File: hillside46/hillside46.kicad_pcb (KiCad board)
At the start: 2 copper layers, 142.5 x 99.9 mm, 86 parts, among them J1 Haptic, J2 TRRS, J3 Bat_Pos, J4 Bat_Neg, J5 Bat_Pos, J6 Bat_Neg, K1 SW_Key, K10 SW_Key, K11 SW_Key, K12 SW_Key, K13 SW_Key, K14 SW_Key, K15 SW_Key, K16 SW_Key, K17 SW_Key, K18 SW_Key, K19 SW_Rotary, K2 SW_Key, K20 SW_Rotary, K21 SW_Key, K22 SW_Key, K23 SW_Key, K3 SW_Key, K4 SW_Key, K5 SW_Key, K6 SW_Key, K7 SW_Key, K8 SW_Key, K9 SW_Key, SW1 SKQGAFE010, SW2 SW_Power, U1 ProMicro_r, U2 SRV05-4

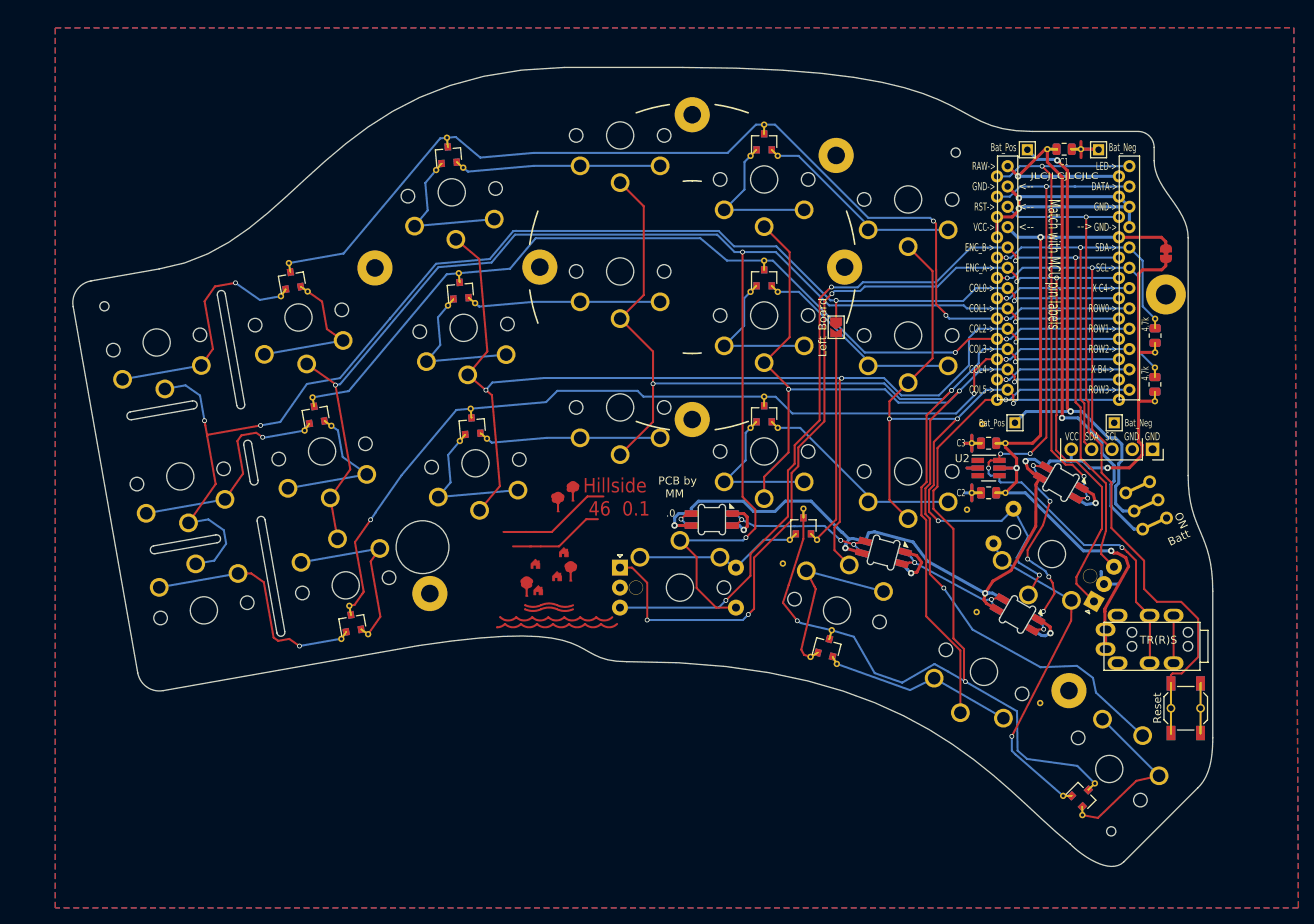
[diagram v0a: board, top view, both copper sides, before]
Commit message: 46 PCB: Ground plane and trace cleanups
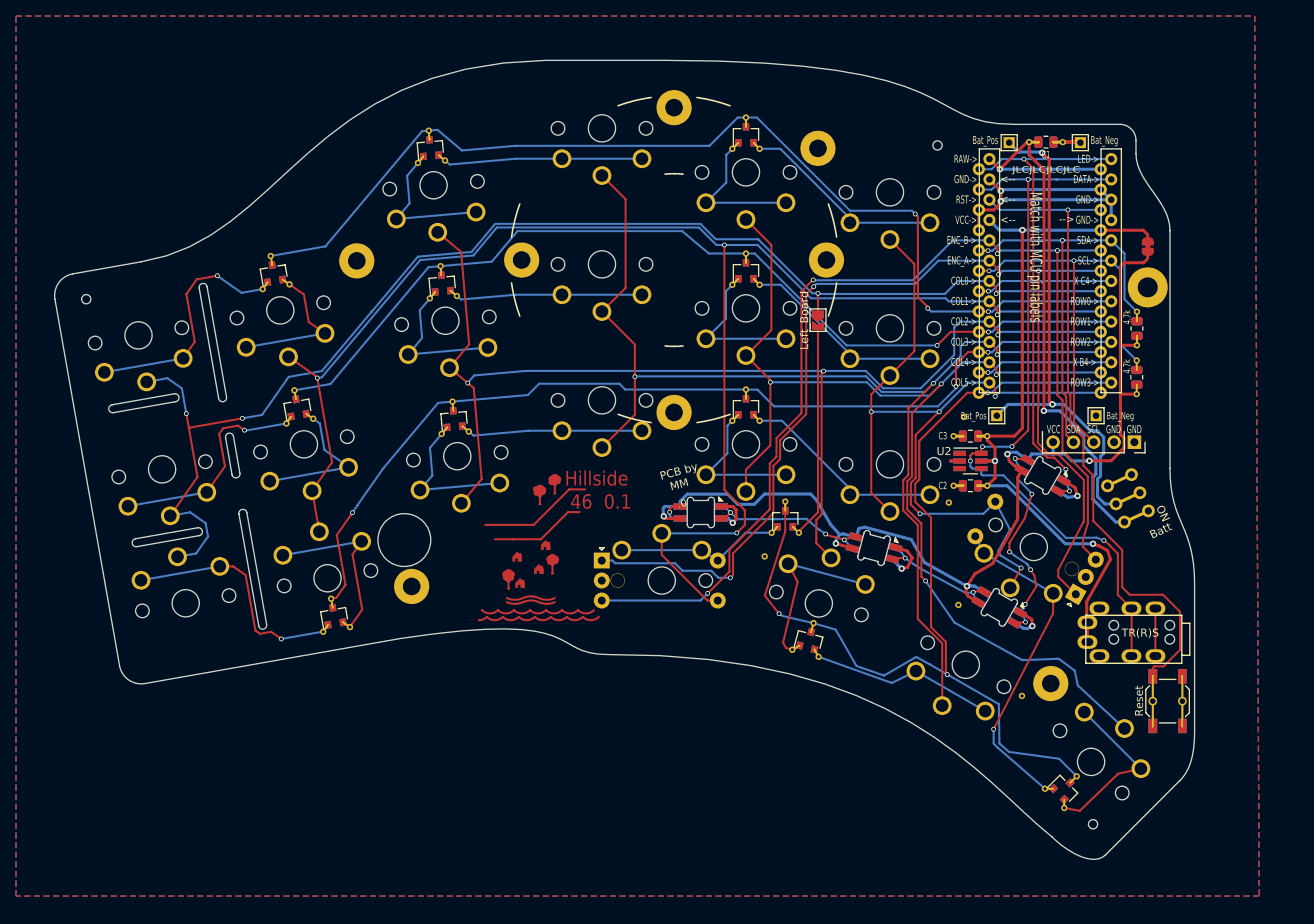
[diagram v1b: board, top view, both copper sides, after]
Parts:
- moved H15 2.93 mm to (93.2, 76.7)
- moved H19 2.73 mm to (194.9, 134.2)
- moved H16 2.65 mm to (203.1, 142.6)
- moved H14 2.61 mm to (132.8, 54.6)
- moved H12 2.57 mm to (88.1, 122.0)
- moved H10 2.48 mm to (80.5, 79.1)
- moved D7 2.44 mm to (101.8, 75.4)
- moved JP1 2.44 mm to (211.1, 72.1)
- moved K19 2.44 mm to (199.1, 105.7)
- moved K21 2.44 mm to (170.0, 116.7)
- moved K22 2.44 mm to (188.4, 124.3)
- moved V5 2.44 mm to (163.2, 110.8)
- moved K5 2.44 mm to (160.9, 62.8)
- moved D13 2.44 mm to (109.4, 118.2)
- moved K3 2.44 mm to (121.8, 64.4)
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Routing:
- net GND: track 85.9 -> 71.6 mm
- net enc_a: track 149.9 -> 141.4 mm, vias 5 -> 4
- net VCC: track 93.2 -> 92.0 mm
- net Net-(D2-Pad2): track 17.3 -> 16.2 mm
- net col1: track 194.3 -> 195.3 mm
- net reset: track 82.4 -> 83.1 mm

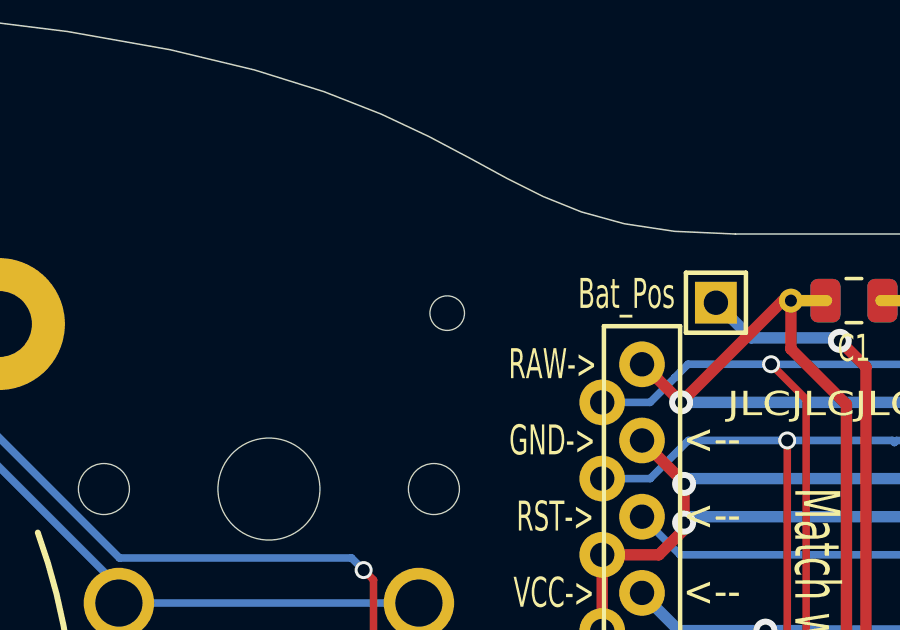
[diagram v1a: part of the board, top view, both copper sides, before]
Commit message: 46 PCB: trace cleanups
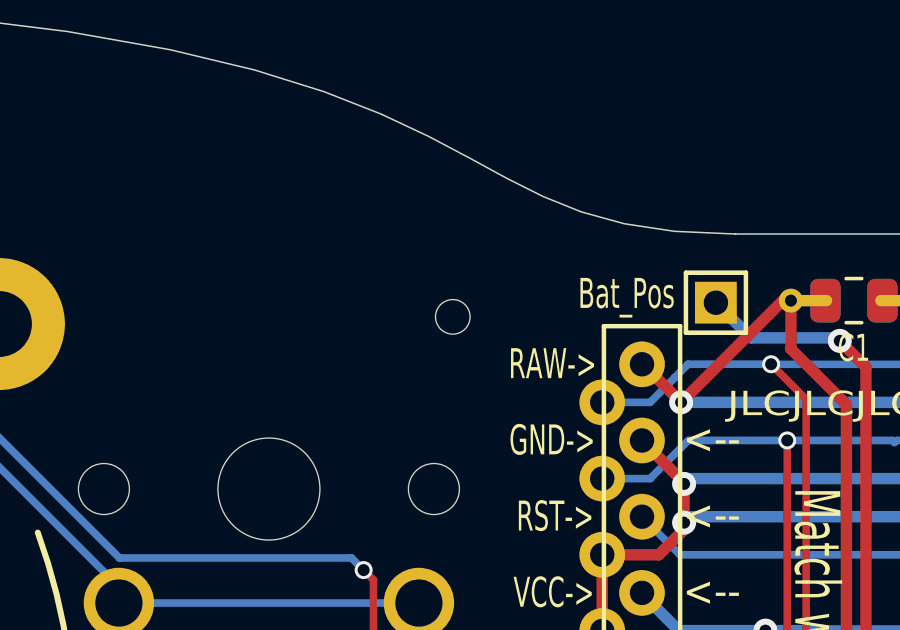
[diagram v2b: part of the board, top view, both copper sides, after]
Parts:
- moved H23 0.22 mm to (185.0, 59.6)
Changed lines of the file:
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@@
   )
   (footprint "hillside_basic:ToolingHole_1.152mm" (layer "F.Cu")
-    (at 184.818727 59.429153)
+    (at 185.004829 59.553153)
     (descr "Mounting Hole 2.1mm, no annular")
     (tags "mounting hole 2.1mm no annular")

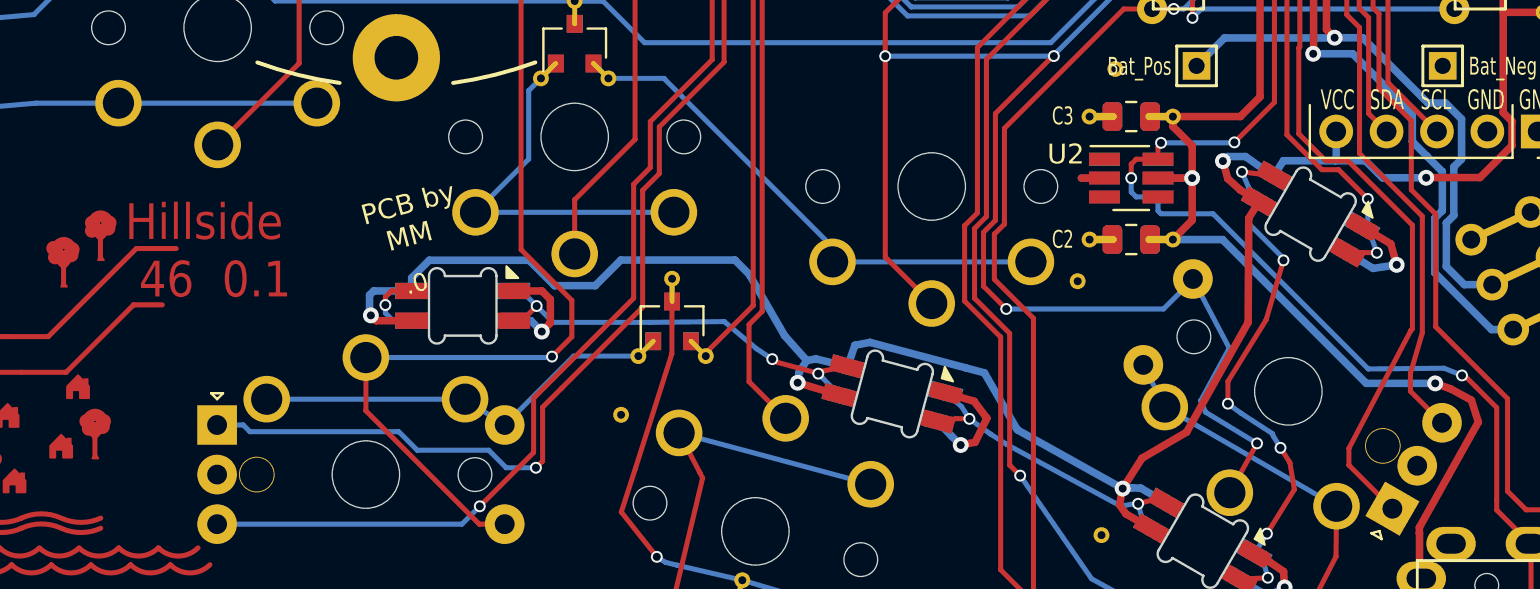
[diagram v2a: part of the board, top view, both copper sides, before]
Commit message: 46: PCB connect ground on encoder. Silk tweaks
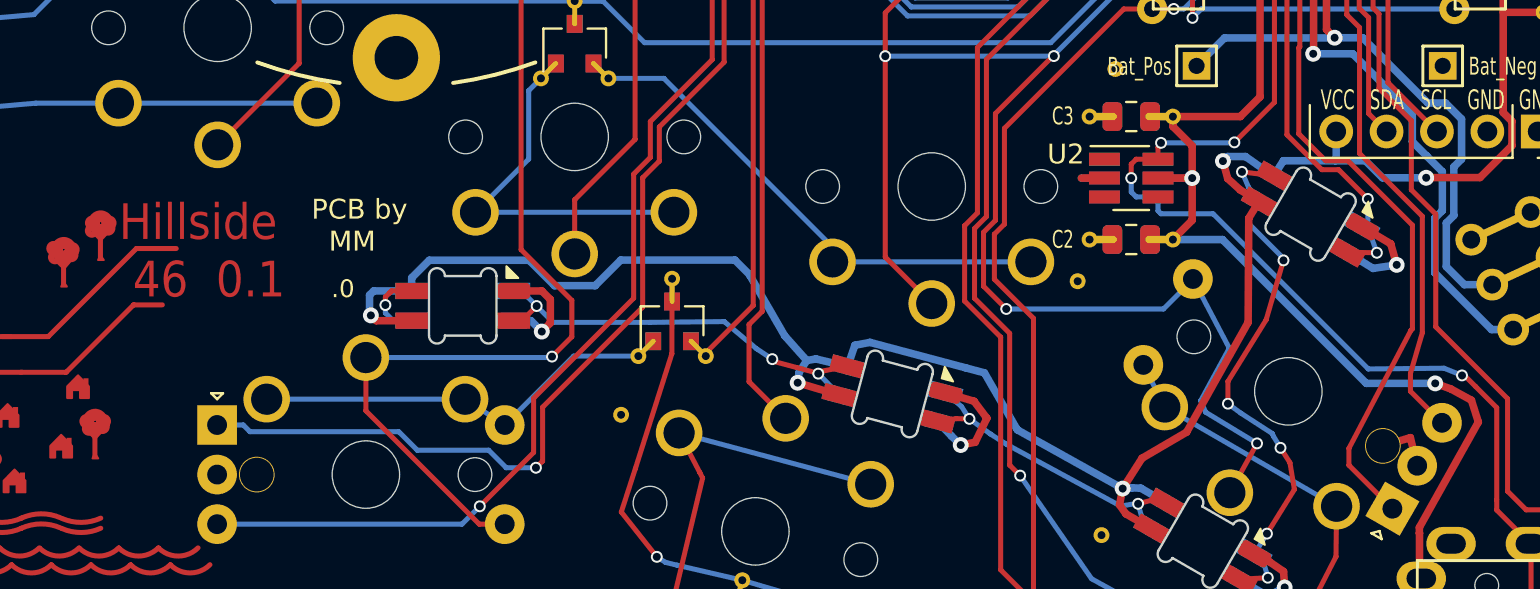
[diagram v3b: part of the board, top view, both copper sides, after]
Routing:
- net GND: track 71.6 -> 74.5 mm
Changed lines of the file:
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@@
   (gr_curve (pts (xy 205.821011 148.110245) (xy 204.095766 149.772261) (xy 200.565772 147.312259) (xy 199.140774 145.87226)) (layer "Edge.Cuts") (width 0.05))
   (gr_arc (start 74.498279 78.666546) (mid 74.953852 76.611692) (end 76.728967 75.480796) (layer "Edge.Cuts") (width 0.05))
-  (gr_text "Hillside \n 46  0.1" (at 138.204829 102.553153) (layer "F.Cu")
+  (gr_text "Hillside \n 46  0.1" (at 137.904829 102.553153) (layer "F.Cu")
     (effects (font (size 1.8 1.6) (thickness 0.24)) (justify left))
   )
-  (gr_text ".0" (at 152.336649 104.340041 15) (layer "F.SilkS")
+  (gr_text ".0" (at 148.604829 104.453153) (layer "F.SilkS")
     (effects (font (size 0.9 0.9) (thickness 0.153)) (justify left))
   )
-  (gr_text "PCB by\n  MM" (at 150.345613 101.562762 15) (layer "F.SilkS")
+  (gr_text "PCB by\n  MM" (at 147.604829 101.253153) (layer "F.SilkS")
     (effects (font (size 1 1) (thickness 0.153)) (justify left))
   )
@@
     (effects (font (size 0.81 1) (thickness 0.15)))
   )
-  (gr_text "Hillside\n 46  0.1" (at 138.204829 102.553153) (layer "F.Mask")
+  (gr_text "Hillside\n 46  0.1" (at 137.904829 102.553153) (layer "F.Mask")
     (effects (font (size 1.8 1.6) (thickness 0.24)) (justify left))
   )
@@
   (segment (start 181.012387 110.119986) (end 179.547645 109.683935) (width 0.381) (layer "F.Cu") (net 11))
   (segment (start 192.715769 65.082257) (end 191.312167 63.67866) (width 0.381) (layer "F.Cu") (net 11))
+  (segment (start 203.004829 111.953153) (end 201.617192 112.369747) (width 0.381) (layer "F.Cu") (net 11))
   (segment (start 192.715771 66.642256) (end 191.873773 67.484258) (width 0.381) (layer "F.Cu") (net 11))
   (segment (start 200.475776 59.012259) (end 202.60578 59.012259) (width 0.381) (layer "F.Cu") (net 11))
+  (segment (start 203.349243 113.369747) (end 203.004829 111.953153) (width 0.381) (layer "F.Cu") (net 11))
   (segment (start 202.605779 59.012259) (end 202.675774 59.082254) (width 0.381) (layer "F.Cu") (net 11))
   (segment (start 200.475771 59.012258) (end 200.485776 59.022259) (width 0.381) (layer "F.Cu") (net 11))
@@
   (segment (start 212.055769 117.302258) (end 212.055769 123.252261) (width 0.254) (layer "F.Cu") (net 22))
   (segment (start 198.733108 97.992117) (end 197.37926 96.638268) (width 0.254) (layer "F.Cu") (net 24))
+  (segment (start 165.142894 96.290565) (end 168.409263 93.024201) (width 0.254) (layer "F.Cu") (net 24))
+  (segment (start 168.409263 93.024201) (end 168.40926 78.01469) (width 0.254) (layer "F.Cu") (net 24))
   (segment (start 203.108107 101.242116) (end 199.858107 97.992116) (width 0.254) (layer "F.Cu") (net 24))
   (segment (start 192.455963 75.56799) (end 192.455959 74.978046) (width 0.254) (layer "F.Cu") (net 24))
-  (segment (start 160.223806 109.453153) (end 164.302896 105.374063) (width 0.254) (layer "F.Cu") (net 24))
   (segment (start 168.40926 78.01469) (end 169.345962 77.077987) (width 0.254) (layer "F.Cu") (net 24))
   (segment (start 199.858107 97.992116) (end 198.733108 97.992117) (width 0.254) (layer "F.Cu") (net 24))
   (segment (start 197.433108 92.247476) (end 197.433108 75.10692) (width 0.254) (layer "F.Cu") (net 24))
-  (segment (start 168.409263 93.024201) (end 168.40926 78.01469) (width 0.254) (layer "F.Cu") (net 24))
   (segment (start 192.455959 74.978046) (end 191.312169 73.834255) (width 0.254) (layer "F.Cu") (net 24))
-  (segment (start 164.302896 99.48407) (end 165.142897 98.644065) (width 0.254) (layer "F.Cu") (net 24))
   (segment (start 202.099243 115.534812) (end 199.908108 113.343675) (width 0.254) (layer "F.Cu") (net 24))
-  (segment (start 158.922327 113.470651) (end 159.258829 113.134149) (width 0.254) (layer "F.Cu") (net 24))
   (segment (start 199.908108 112.492117) (end 203.033108 106.542116) (width 0.254) (layer "F.Cu") (net 24))
-  (segment (start 165.142897 98.644065) (end 165.142894 96.290565) (width 0.254) (layer "F.Cu") (net 24))
   (segment (start 197.433108 75.10692) (end 197.435772 75.104256) (width 0.254) (layer "F.Cu") (net 24))
-  (segment (start 164.302896 105.374063) (end 164.302896 99.48407) (width 0.254) (layer "F.Cu") (net 24))
-  (segment (start 159.258829 110.41813) (end 160.223806 109.453153) (width 0.254) (layer "F.Cu") (net 24))
+  (segment (start 159.258829 110.41813) (end 164.302896 105.374063) (width 0.254) (layer "F.Cu") (net 24))
+  (segment (start 164.302896 98.855086) (end 165.142894 98.015088) (width 0.254) (layer "F.Cu") (net 24))
   (segment (start 203.033108 106.542116) (end 203.108108 106.467117) (width 0.254) (layer "F.Cu") (net 24))
+  (segment (start 159.258829 113.134149) (end 159.258829 110.41813) (width 0.254) (layer "F.Cu") (net 24))
+  (segment (start 164.302896 105.374063) (end 164.302896 98.855086) (width 0.254) (layer "F.Cu") (net 24))
+  (segment (start 165.142894 98.015088) (end 165.142894 96.290565) (width 0.254) (layer "F.Cu") (net 24))
   (segment (start 197.37926 92.301324) (end 197.433108 92.247476) (width 0.254) (layer "F.Cu") (net 24))
-  (segment (start 159.258829 113.134149) (end 159.258829 110.41813) (width 0.254) (layer "F.Cu") (net 24))
   (segment (start 197.37926 96.638268) (end 197.37926 92.301324) (width 0.254) (layer "F.Cu") (net 24))
   (segment (start 203.108108 106.467117) (end 203.108107 101.242116) (width 0.254) (layer "F.Cu") (net 24))
+  (segment (start 158.922327 113.470651) (end 159.258829 113.134149) (width 0.254) (layer "F.Cu") (net 24))
   (segment (start 199.908108 113.343675) (end 199.908108 112.492117) (width 0.254) (layer "F.Cu") (net 24))
-  (segment (start 165.142894 96.290565) (end 168.409263 93.024201) (width 0.254) (layer "F.Cu") (net 24))
   (via (at 197.435772 75.104256) (size 0.6) (drill 0.4) (layers "F.Cu" "B.Cu") (net 24))
   (via (at 158.922327 113.470651) (size 0.6) (drill 0.4) (layers "F.Cu" "B.Cu") (net 24))
@@
   (segment (start 184.923727 73.834255) (end 191.312169 73.834255) (width 0.254) (layer "B.Cu") (net 24))
   (segment (start 169.685963 76.737987) (end 182.019995 76.737987) (width 0.254) (layer "B.Cu") (net 24))
-  (segment (start 169.235965 76.237987) (end 167.809747 77.6642) (width 0.254) (layer "F.Cu") (net 25))
   (segment (start 192.292895 72.27498) (end 191.312175 71.294254) (width 0.254) (layer "F.Cu") (net 25))
+  (segment (start 200.442287 97.626296) (end 200.442287 91.276296) (width 0.254) (layer "F.Cu") (net 25))
+  (segment (start 164.689379 96.01759) (end 164.689379 97.826551) (width 0.254) (layer "F.Cu") (net 25))
   (segment (start 169.28596 76.237994) (end 169.235965 76.237987) (width 0.254) (layer "F.Cu") (net 25))
-  (segment (start 200.442287 97.626296) (end 200.442287 91.276296) (width 0.254) (layer "F.Cu") (net 25))
-  (segment (start 167.80975 92.89722) (end 164.689379 96.01759) (width 0.254) (layer "F.Cu") (net 25))
-  (segment (start 158.804829 109.96862) (end 158.804829 112.702144) (width 0.254) (layer "F.Cu") (net 25))
-  (segment (start 164.689379 96.01759) (end 164.689376 98.337588) (width 0.254) (layer "F.Cu") (net 25))
   (segment (start 203.008108 109.613548) (end 203.008107 108.717117) (width 0.254) (layer "F.Cu") (net 25))
+  (segment (start 164.689379 97.826551) (end 163.84938 98.66655) (width 0.254) (layer "F.Cu") (net 25))
+  (segment (start 158.804829 112.702144) (end 156.092901 115.414072) (width 0.254) (layer "F.Cu") (net 25))
   (segment (start 203.008107 108.717117) (end 203.608108 106.667116) (width 0.254) (layer "F.Cu") (net 25))
   (segment (start 200.883108 98.067116) (end 200.442287 97.626296) (width 0.254) (layer "F.Cu") (net 25))
-  (segment (start 158.804829 112.702144) (end 156.092901 115.414072) (width 0.254) (layer "F.Cu") (net 25))
-  (segment (start 163.84938 104.924069) (end 158.804829 109.96862) (width 0.254) (layer "F.Cu") (net 25))
+  (segment (start 158.804829 109.96862) (end 158.804829 112.702144) (width 0.254) (layer "F.Cu") (net 25))
+  (segment (start 169.235965 76.237987) (end 167.809747 77.6642) (width 0.254) (layer "F.Cu") (net 25))
+  (segment (start 167.80975 92.89722) (end 164.689379 96.01759) (width 0.254) (layer "F.Cu") (net 25))
   (segment (start 192.292896 72.964065) (end 192.292895 72.27498) (width 0.254) (layer "F.Cu") (net 25))
-  (segment (start 164.689376 98.337588) (end 163.849383 99.177589) (width 0.254) (layer "F.Cu") (net 25))
-  (segment (start 163.849383 99.177589) (end 163.84938 104.924069) (width 0.254) (layer "F.Cu") (net 25))
   (segment (start 203.608108 100.792117) (end 200.883108 98.067116) (width 0.254) (layer "F.Cu") (net 25))
+  (segment (start 163.84938 98.66655) (end 163.84938 104.924069) (width 0.254) (layer "F.Cu") (net 25))
   (segment (start 204.599243 111.204684) (end 203.008108 109.613548) (width 0.254) (layer "F.Cu") (net 25))
   (segment (start 203.608108 106.667116) (end 203.608108 100.792117) (width 0.254) (layer "F.Cu") (net 25))
   (segment (start 199.799271 90.63328) (end 199.799272 72.564257) (width 0.254) (layer "F.Cu") (net 25))
+  (segment (start 200.442287 91.276296) (end 199.820608 90.654617) (width 0.254) (layer "F.Cu") (net 25))
+  (segment (start 163.84938 104.924069) (end 158.804829 109.96862) (width 0.254) (layer "F.Cu") (net 25))
+  (segment (start 199.820608 90.654617) (end 199.799271 90.63328) (width 0.254) (layer "F.Cu") (net 25))
   (segment (start 167.809747 77.6642) (end 167.80975 92.89722) (width 0.254) (layer "F.Cu") (net 25))
-  (segment (start 200.442287 91.276296) (end 199.820608 90.654617) (width 0.254) (layer "F.Cu") (net 25))
-  (segment (start 199.820608 90.654617) (end 199.799271 90.63328) (width 0.254) (layer "F.Cu") (net 25))
   (via (at 199.799272 72.564257) (size 0.6) (drill 0.4) (layers "F.Cu" "B.Cu") (net 25))
   (via (at 192.292896 72.964065) (size 0.6) (drill 0.4) (layers "F.Cu" "B.Cu") (net 25))
